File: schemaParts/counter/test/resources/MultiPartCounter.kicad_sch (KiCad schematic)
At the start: 8 parts, among them U1 74LS92

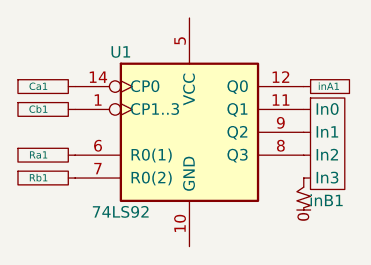
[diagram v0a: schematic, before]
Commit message: Fix UnitTest for MultiPart Counter. Fixes in MultiPart Counter.
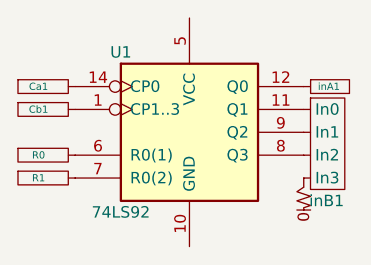
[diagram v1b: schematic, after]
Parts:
- renumbered Ra1 to R0, Rb1 to R1
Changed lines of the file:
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@@
     (pin "1")
     (instances
-      (project "MultiUnitCounter"
+      (project "MultiPartCounter"
         (path "/dca00733-6e59-4b89-b3a6-bb50926963b6"
           (reference "pulldown1") (unit 1)
@@
     (pin "1")
     (instances
-      (project "MultiUnitCounter"
+      (project "MultiPartCounter"
         (path "/dca00733-6e59-4b89-b3a6-bb50926963b6"
           (reference "inA1") (unit 1)
@@
     (pin "0")
     (instances
-      (project "MultiUnitCounter"
+      (project "MultiPartCounter"
         (path "/dca00733-6e59-4b89-b3a6-bb50926963b6"
           (reference "inB1") (unit 1)
@@
     (pin "6")
     (instances
-      (project "MultiUnitCounter"
+      (project "MultiPartCounter"
         (path "/dca00733-6e59-4b89-b3a6-bb50926963b6"
           (reference "U1") (unit 1)
@@
     (pin "1")
     (instances
-      (project "MultiUnitCounter"
+      (project "MultiPartCounter"
         (path "/dca00733-6e59-4b89-b3a6-bb50926963b6"
           (reference "Cb1") (unit 1)
@@
     (pin "1")
     (instances
-      (project "MultiUnitCounter"
+      (project "MultiPartCounter"
         (path "/dca00733-6e59-4b89-b3a6-bb50926963b6"
           (reference "Ca1") (unit 1)
@@
   (symbol (lib_id "Tests:OutPin") (at 114.3 78.74 0) (unit 1)
     (in_bom yes) (on_board yes) (dnp no)
-    (property "Reference" "Rb1" (at 110.236 78.74 0)
+    (property "Reference" "R1" (at 110.236 78.74 0)
       (effects (font (size 0.8 0.8)))
     )
@@
     (pin "1")
     (instances
-      (project "MultiUnitCounter"
+      (project "MultiPartCounter"
         (path "/dca00733-6e59-4b89-b3a6-bb50926963b6"
-          (reference "Rb1") (unit 1)
+          (reference "R1") (unit 1)
         )
       )
@@
   (symbol (lib_id "Tests:OutPin") (at 114.3 76.2 0) (unit 1)
     (in_bom yes) (on_board yes) (dnp no)
-    (property "Reference" "Ra1" (at 110.236 76.2 0)
+    (property "Reference" "R0" (at 110.236 76.2 0)
       (effects (font (size 0.8 0.8)))
     )
@@
     (pin "1")
     (instances
-      (project "MultiUnitCounter"
+      (project "MultiPartCounter"
         (path "/dca00733-6e59-4b89-b3a6-bb50926963b6"
-          (reference "Ra1") (unit 1)
+          (reference "R0") (unit 1)
         )
       )
